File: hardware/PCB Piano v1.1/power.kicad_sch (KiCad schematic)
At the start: 51 parts, among them CON1 254, J1 USB_C_Receptacle_USB2.0_16P, J4 Conn_01x02_Pin, J5 Conn_01x02_Pin, SW1 MFS126D, U12 TLV73318PDBV, U3 BQ24072RGT, U8 TPS63001, U9 TPS61023

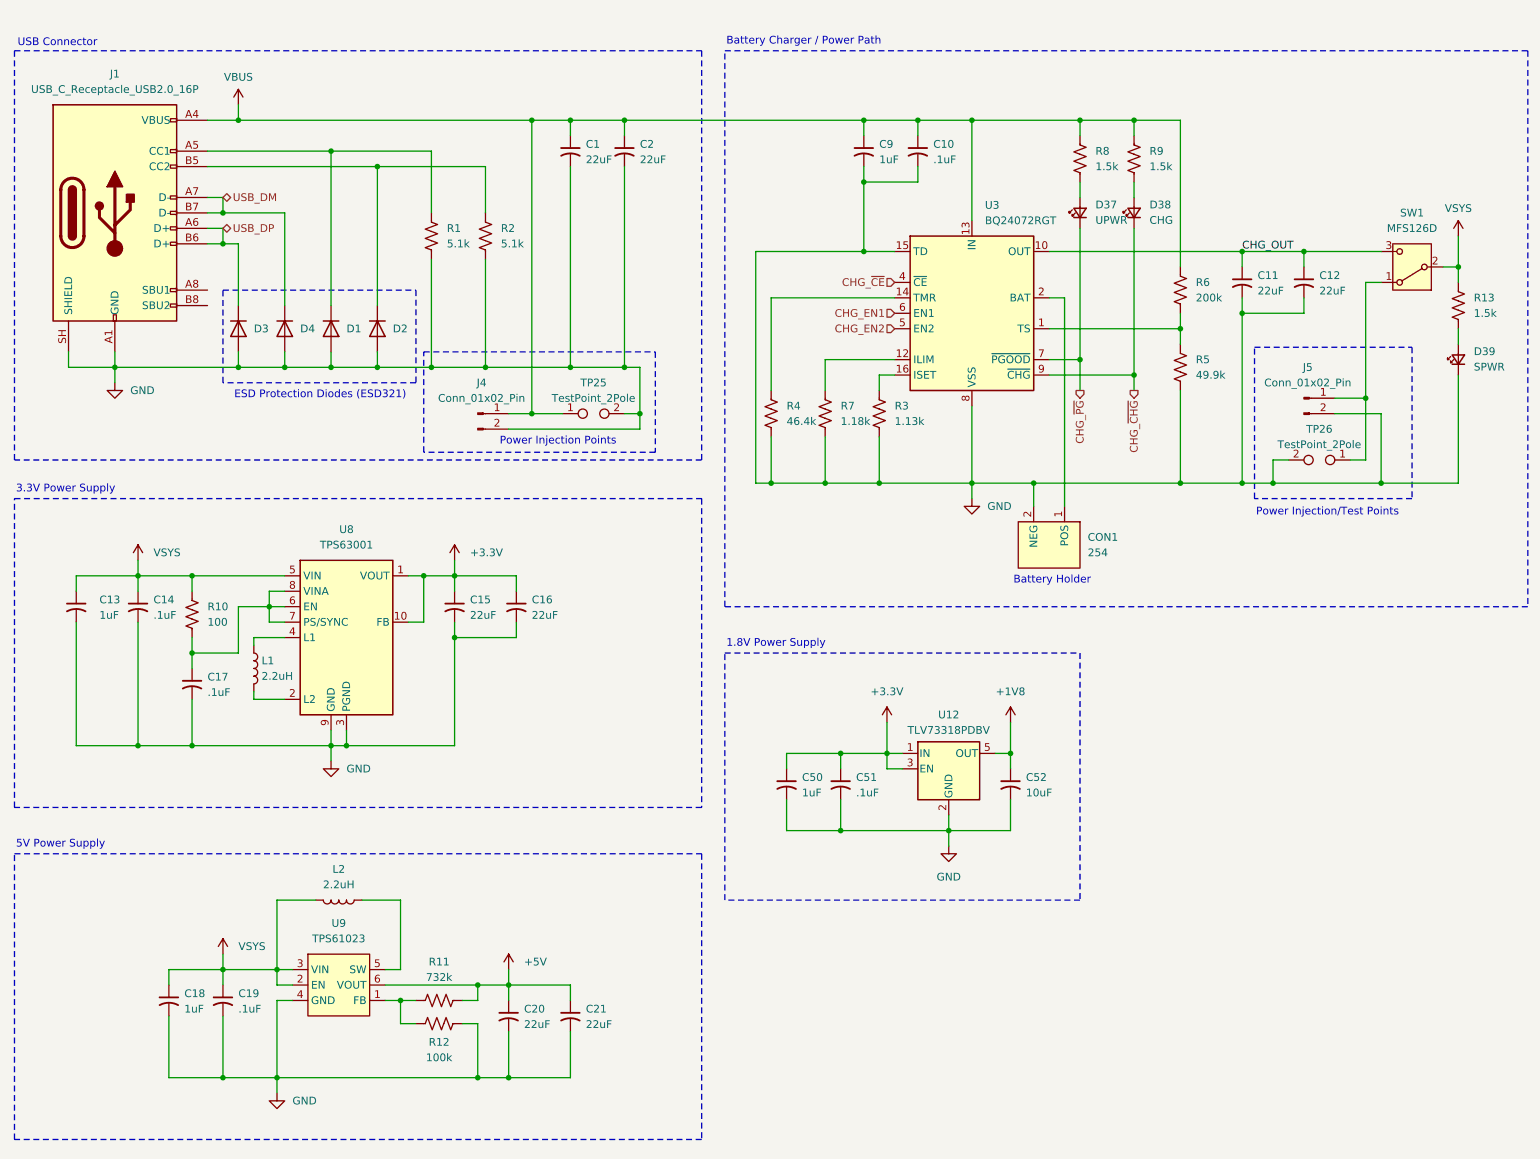
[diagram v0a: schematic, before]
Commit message: Development Phase - PCB Complete - ERC/DRC in progress
Development commit. PBC layout complete. ERC/DRC checks in progress. Swapped some connectors for JST connectors with Adafruit-style polarization.
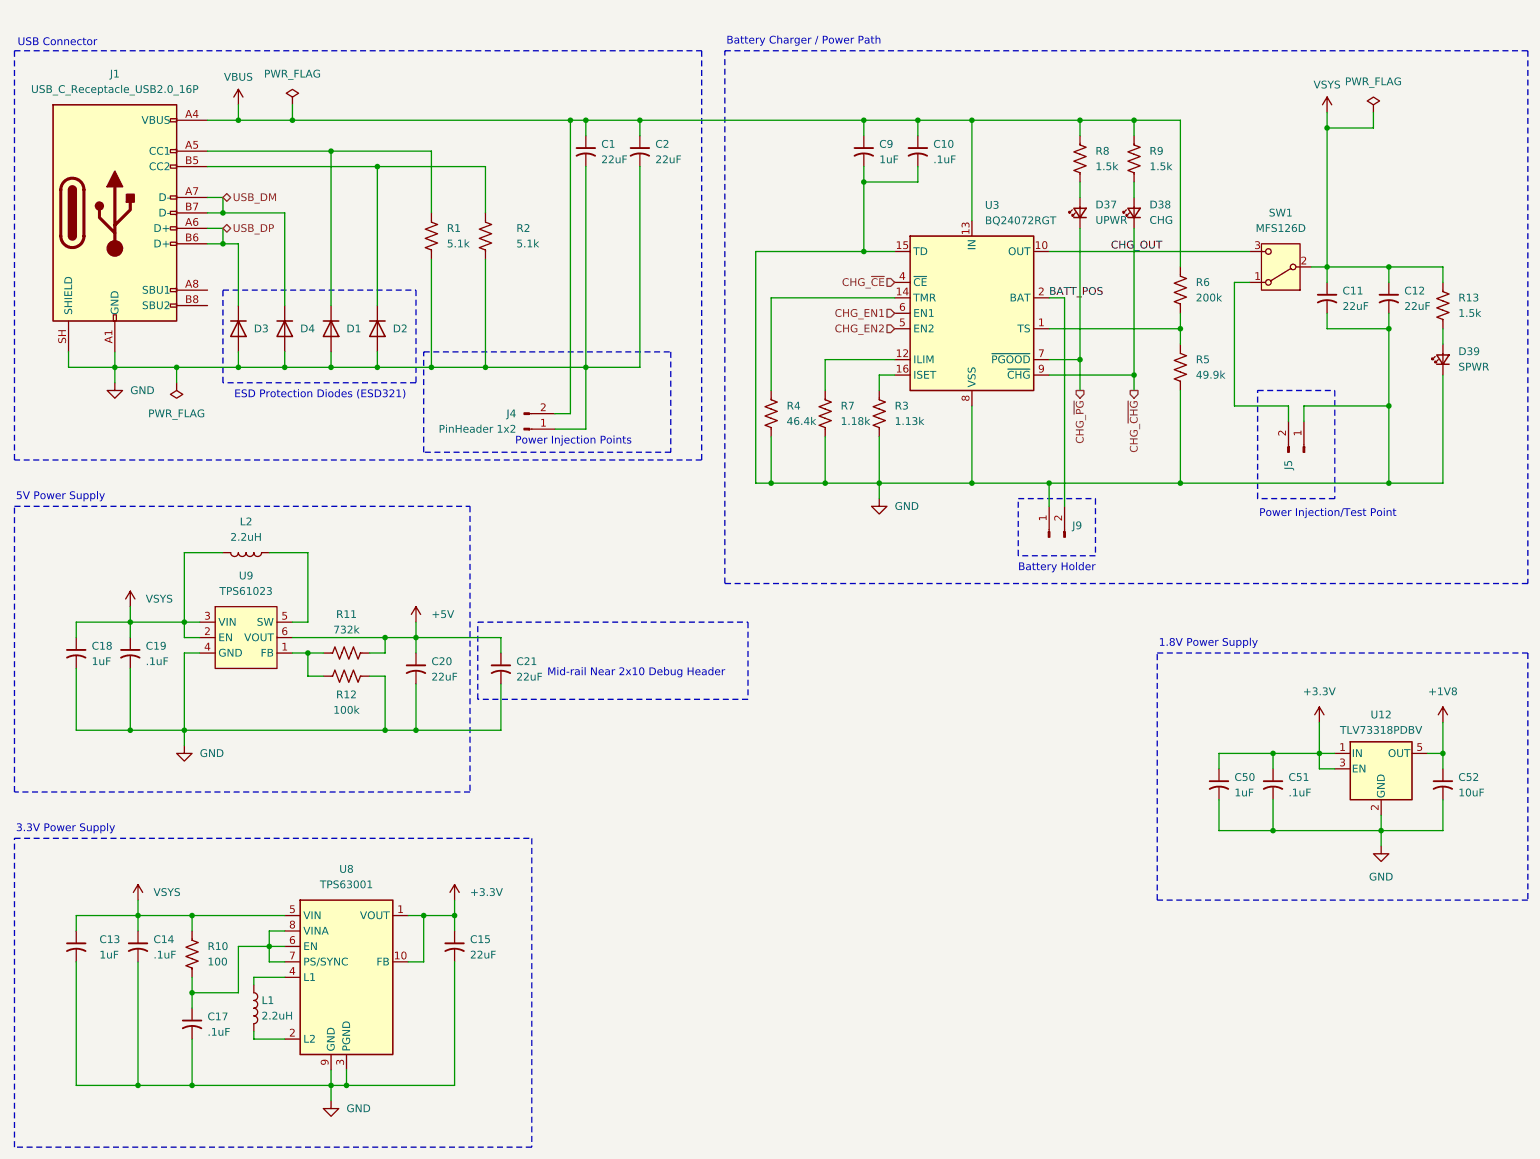
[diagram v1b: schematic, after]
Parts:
- removed C16: 22uF, Capacitor_Tantalum_SMD:CP_EIA-6032-20_AVX-F, symbol Device:C_Small_US
- removed CON1: 254, PCBPiano_Footprints:BatteryHolder_254Clips_18650Battery, symbol PCB Piano Symbols:254
- removed TP25, TP26: TestPoint_2Pole, PCBPiano_Footprints:TestPoint_2Pads_2.5mmx2.5mm_5mmSpacing, symbol Connector:TestPoint_2Pole
- added J9: (no value), Connector_JST:JST_PH_B2B-PH-SM4-TB_1x02-1MP_P2.00mm_Vertical, symbol Connector:Conn_01x02_Pin
- J4: value Conn_01x02_Pin -> PinHeader 1x2
- J5: value Conn_01x02_Pin -> (none)
- SW1: footprint PCBPiano_Footprints:SolderPoint_3Pads_2.54x2.54_5.08Spacing -> Connector_JST:JST_PH_B3B-PH-SM4-TB_1x03-1MP_P2.00mm_Vertical
- U9: symbol texas_instruments:TPS61023 -> PCB Piano Symbols:TPS61023
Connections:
- net CHG_OUT: no longer C11.1, C12.1
- net GND: now also J4.1 (Pin_1), J5.1 (Pin_1), J9.1 (Pin_1); no longer J4.2 (Pin_2), J5.2 (Pin_2)
- net VBUS: now also J4.2 (Pin_2); no longer J4.1 (Pin_1)
- net VSYS: now also C11.1, C12.1
- net BATT_POS: now reaches U3.2 (BAT), U3.3 (BAT)
- net BATT_POS: now also J9.2 (Pin_2)
- net at SW1.1 (A): now also J5.2 (Pin_2); no longer J5.1 (Pin_1)
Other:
- note added: "Mid-rail Near 2x10 Debug Header"
- note added: "Power Injection/Test Point"
- note removed: "Power Injection/Test Points"
- moved on the sheet: C1, C11, C12, C13, C14, C15, C17, C18, C19, C2, C20, C21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

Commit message: Firmware architecture complete - PCB revision with new charger.
Firmware Architecture Complete

- Added MP2724 charger driver
- Added TLV320DAC3100 driver
- Added MTCH2120 touch driver
- Added PCA9685 driver
- Added DotStar driver
- Added rotary encoder driver
- Added touch and LED maps
- Added control/audio/voice managers
- Added audio command queue
- Added Core1 audio architecture
- Added status LED system
- Added LED animation framework

Changes hardware schematic and PCB to accommodate a newer-style USB-C sink battery charger chip and USB data MUX to protect MCU while powered off.
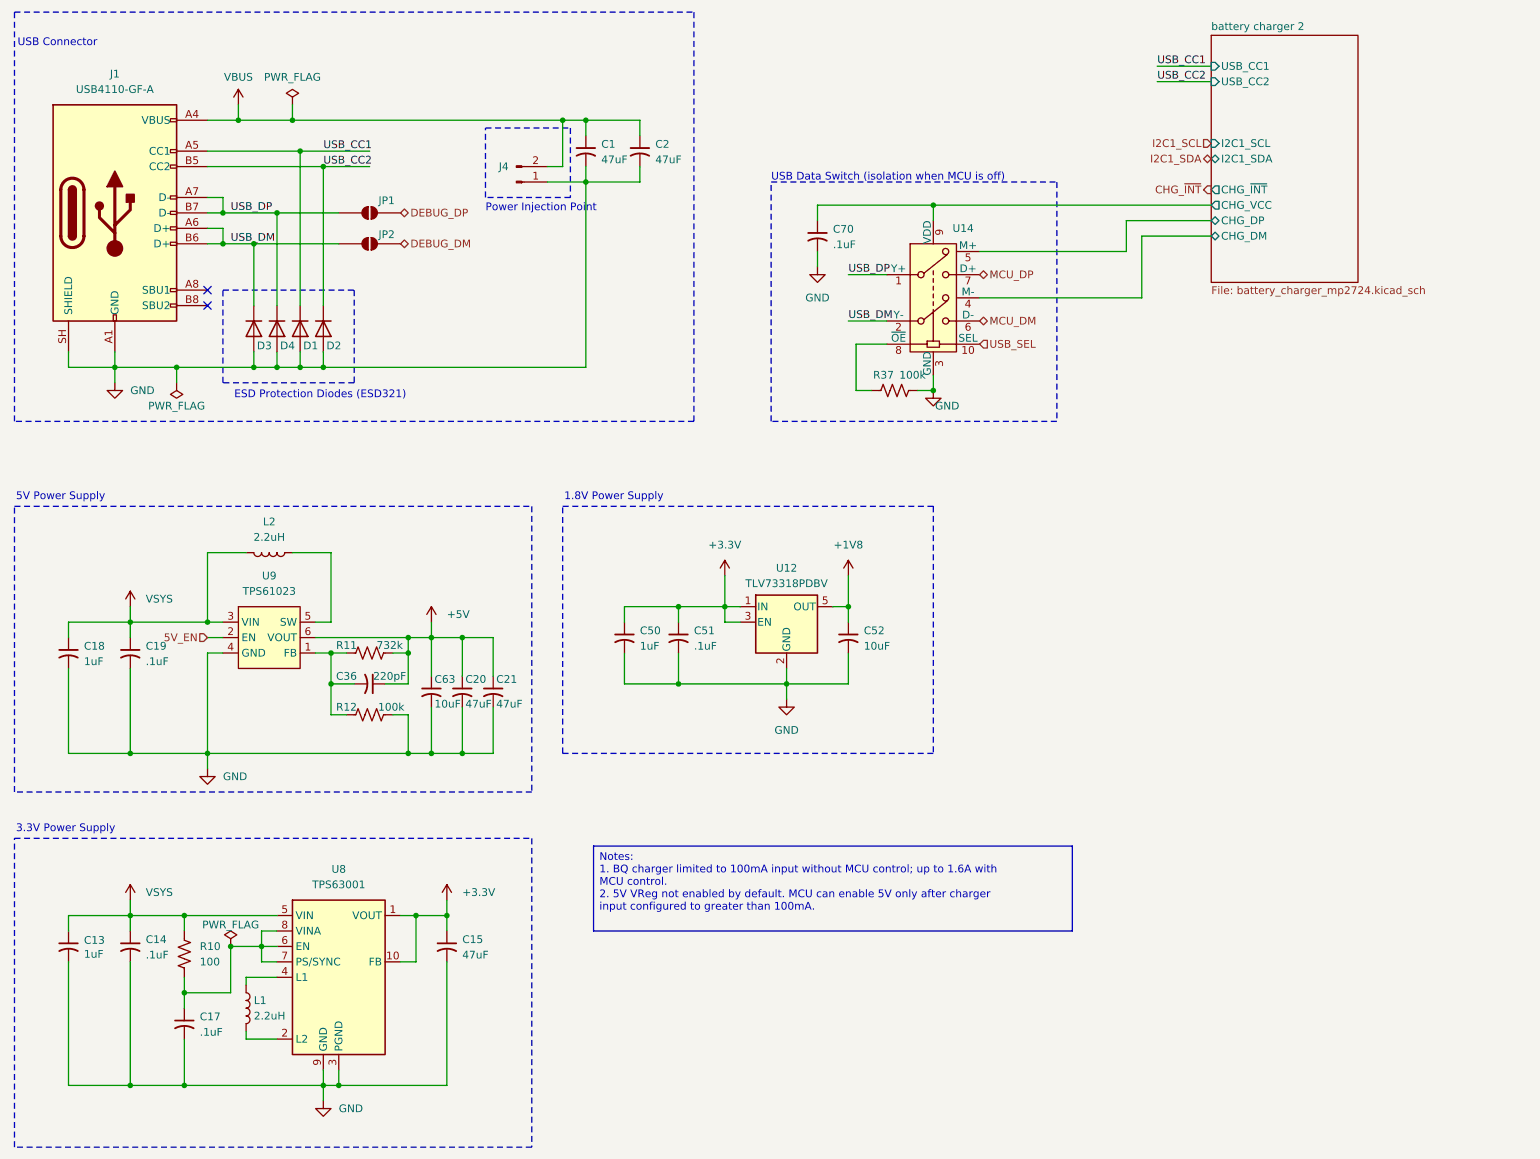
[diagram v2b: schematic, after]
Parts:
- removed C10: .1uF, Capacitor_SMD:C_0603_1608Metric, symbol Device:C_Small_US
- removed C11, C12: 22uF, Capacitor_Tantalum_SMD:CP_EIA-6032-20_AVX-F, symbol Device:C_Small_US
- removed C9: 1uF, Capacitor_SMD:C_0603_1608Metric, symbol Device:C_Small_US
- removed D37: UPWR, LED_SMD:LED_0603_1608Metric, symbol Device:LED_Small
- removed D38: CHG, LED_SMD:LED_0603_1608Metric, symbol Device:LED_Small
- removed D39: SPWR, LED_SMD:LED_0603_1608Metric, symbol Device:LED_Small
- removed J5: (no value), Connector_PinHeader_2.54mm:PinHeader_1x02_P2.54mm_Vertical_SMD_Pin1Left, symbol Connector:Conn_01x02_Pin
- removed J9: (no value), Connector_JST:JST_PH_B2B-PH-SM4-TB_1x02-1MP_P2.00mm_Vertical, symbol Connector:Conn_01x02_Pin
- removed R1, R2: 5.1k, Resistor_SMD:R_0603_1608Metric, symbol Device:R_US
- removed R13, R8, R9: 1.5k, Resistor_SMD:R_0603_1608Metric, symbol Device:R_US
- removed R3: 1.13k, Resistor_SMD:R_0603_1608Metric, symbol Device:R_US
- removed R4: 46.4k, Resistor_SMD:R_0603_1608Metric, symbol Device:R_US
- removed R5: 49.9k, Resistor_SMD:R_0603_1608Metric, symbol Device:R_US
- removed R6: 200k, Resistor_SMD:R_0603_1608Metric, symbol Device:R_US
- removed R7: 1.18k, Resistor_SMD:R_0603_1608Metric, symbol Device:R_US
- removed SW1: MFS126D, Connector_JST:JST_PH_B3B-PH-SM4-TB_1x03-1MP_P2.00mm_Vertical, symbol Switch:SW_SPDT
- removed U3: BQ24072RGT, Package_DFN_QFN:VQFN-16-1EP_3x3mm_P0.5mm_EP1.6x1.6mm, symbol Battery_Management:BQ24072RGT
- added C36: 220pF, Capacitor_SMD:C_0603_1608Metric, symbol Device:C_Small_US
- added C63: 10uF, Capacitor_SMD:C_0805_2012Metric, symbol Device:C_Small_US
- added C70: .1uF, Capacitor_SMD:C_0603_1608Metric, symbol Device:C_Small_US
- added JP1, JP2: SolderJumper_2_Open, Jumper:SolderJumper-2_P1.3mm_Open_RoundedPad1.0x1.5mm, symbol Jumper:SolderJumper_2_Open
- added R37: 100k, Resistor_SMD:R_0603_1608Metric, symbol Device:R_US
- added U14: PI3USB102G, PCBPiano_Footprints:TQFN-10_ZL_1.6x1.3mm_P0.4mm, symbol PCB_Piano_Symbols:Switch_USB_Data_Dual_SPDT_PI3USB102G
- C1, C15, C2, C20, C21: value 22uF -> 47uF; footprint Capacitor_Tantalum_SMD:CP_EIA-6032-20_AVX-F -> Capacitor_Tantalum_SMD:CP_EIA-3528-15_AVX-H
- C52: footprint Capacitor_SMD:C_0603_1608Metric -> Capacitor_SMD:C_0805_2012Metric
- D1, D2, D3, D4: value (none) -> ESD321; footprint Diode_SMD:D_SOD-523 -> PCBPiano_Footprints:D_SOD-523
- J1: value USB_C_Receptacle_USB2.0_16P -> USB4110-GF-A; footprint Connector_USB:USB_C_Receptacle_GCT_USB4110 -> PCBPiano_Footprints:USB_C_Receptacle_GCT_USB4110
- J4: value PinHeader 1x2 -> PinHeader 1x02 SMT
- L1: footprint Inductor_SMD:L_1008_2520Metric -> PCBPiano_Footprints:L_Bourns_SRP4020T_4.06x4.45x2.0mm
- L2: footprint Inductor_SMD:L_1008_2520Metric -> PCBPiano_Footprints:L_Pulse_BMRB00060630_7.3x6.6mm
- U8: footprint Package_SON:Texas_DRC0010J_ThermalVias -> PCBPiano_Footprints:Texas_DRC0010J
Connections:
- net +5V: now also C36.1, C63.1
- net GND: now also C63.2, C70.2, R37.1, U14.3 (GND)
- net USB_DM: now also D3.1 (K), J1.A6 (D+), J1.B6 (D+), JP2.1 (A), U14.2 (Y-); no longer D4.1 (K), J1.A7 (D-), J1.B7 (D-)
- net USB_DP: now also D4.1 (K), J1.A7 (D-), J1.B7 (D-), JP1.1 (A), U14.1 (Y+); no longer D3.1 (K), J1.A6 (D+), J1.B6 (D+)
- net VSYS: no longer U9.2 (EN)
- net USB_CC1: now reaches D1.1 (K), J1.A5 (CC1)
- net at R11.2, R12.2, U9.1 (FB): now also C36.2
- net USB_CC2: now reaches D2.1 (K), J1.B5 (CC2)
- new net: R37.2, U14.8 (~{OE})
- new net 5V_EN: U9.2 (EN)
- new net DEBUG_DM: JP2.2 (B)
- new net DEBUG_DP: JP1.2 (B)
- new net MCU_DM: U14.6 (D-)
- new net MCU_DP: U14.7 (D+)
- new net USB_SEL: U14.10 (SEL)
- new net battery charger 2/CHG_DM: U14.4 (M-)
- new net battery charger 2/CHG_DP: U14.5 (M+)
- new net battery charger 2/CHG_VCC: C70.1, U14.9 (VDD)
- no-connect marks 0 -> 2
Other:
- added sheet battery charger 2 (battery_charger_mp2724.kicad_sch)
- note added: "Power Injection Point"
- note added: "USB Data Switch (isolation when MCU is off)"
- note removed: "Battery Charger / Power Path"
- note removed: "Battery Holder"
- note removed: "Mid-rail Near 2x10 Debug Header"
- note removed: "Power Injection Points"
- note removed: "Power Injection/Test Point"
- moved on the sheet: C13, C14, C15, C17, C18, C20, C50, C51, C52, D1, D2, D3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

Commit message: PCB Finalized and Ordered. Firmware near completion.
PCB Finalized and Ordered. Final revisions included fixing bugs on some peripheral chips. Also added an RTC circuit after realizing the SD card could benefit from adding file timestamps.

Firmware near completion. Still need to finalize some SD card operations. Synth audio core is finished and all the board peripheral chip drivers were completed.
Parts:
- removed C2: 47uF, Capacitor_Tantalum_SMD:CP_EIA-3528-15_AVX-H, symbol Device:C_Small_US
- added C78, C79: 47uF, Capacitor_Tantalum_SMD:CP_EIA-3528-15_AVX-H, symbol Device:C_Small_US
- added D45: 3.3Vf, 104mcd, PCBPiano_Footprints:LED_0603_1608Metric, symbol Device:LED_Small
- added J5: PinHeader 1x02 SMT, Connector_PinHeader_2.54mm:PinHeader_1x02_P2.54mm_Vertical_SMD_Pin1Right, symbol Connector:Conn_01x02_Pin
- added R77: 1.5k, Resistor_SMD:R_0603_1608Metric, symbol Device:R_US
- added SW1: JST-PH 1x03 SMT, Connector_JST:JST_PH_B3B-PH-SM4-TB_1x03-1MP_P2.00mm_Vertical, symbol PCB Piano Symbols:SW_SPDT_MP
- C1: footprint Capacitor_Tantalum_SMD:CP_EIA-3528-15_AVX-H -> Capacitor_Tantalum_SMD:CP_EIA-7343-43_Kemet-X; DigiKey_Part_Number (none) -> TAJB476K010RNJ; Manufacturer Part Number (none) -> TAJB476K010RNJ; Volt Rating (none) -> 25V
- C13, C18, C50: DigiKey_Part_Number (none) -> 1276-1184-1-ND; Manufacturer Part Number (none) -> CL10B105KA8NNNC; Volt Rating (none) -> 10V
- C14, C17, C19, C51, C70: DigiKey_Part_Number (none) -> 1276-1935-2-ND; Manufacturer Part Number (none) -> CL10B104KB8NNWC; Volt Rating (none) -> 10V
- C15, C20, C21: DigiKey_Part_Number (none) -> TAJB476K010RNJ; Manufacturer Part Number (none) -> TAJB476K010RNJ; Volt Rating (none) -> 10V
- C36: DigiKey_Part_Number (none) -> 478-KGM15ACG1E221JTCT-ND; Manufacturer Part Number (none) -> KGM15ACG1E221JT; Volt Rating (none) -> 10V
- C52, C63: DigiKey_Part_Number (none) -> 490-10516-1-ND; Manufacturer Part Number (none) -> GRM21BR71A106KA73L GRM21BR71A106KA73L GRM21BR71A106KA73L GR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; Volt Rating (none) -> 10V
- D1, D2, D3, D4: DigiKey_Part_Number (none) -> ESD321; Manufacturer Part Number (none) -> ESD321
- J1: DigiKey_Part_Number (none) -> USB4110-GF-A; Manufacturer Part Number (none) -> USB4110-GF-A
- J4: footprint Connector_PinHeader_2.54mm:PinHeader_1x02_P2.54mm_Vertical_SMD_Pin1Left -> Connector_PinHeader_2.54mm:PinHeader_1x02_P2.54mm_Vertical_SMD_Pin1Right
- JP1, JP2: footprint Jumper:SolderJumper-2_P1.3mm_Open_RoundedPad1.0x1.5mm -> PCBPiano_Footprints:SolderJumper-2_P1.3mm_Open_RoundedPad1.0x1.5mm
- U12: value TLV73318PDBV -> 1.8V; DigiKey_Part_Number (none) -> TLV73318PDBV; Manufacturer Part Number (none) -> TLV73318PDBV
- U14: value PI3USB102G -> 1:2 USB MUX; DigiKey_Part_Number (none) -> PI3USB102G; Manufacturer Part Number (none) -> PI3USB102G
- U8: value TPS63001 -> 3.3V; DigiKey_Part_Number (none) -> TPS63001; Manufacturer Part Number (none) -> TPS63001
- U9: value TPS61023 -> 5V; DigiKey_Part_Number (none) -> TPS61023; Manufacturer Part Number (none) -> TPS61023
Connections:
- net DEBUG_DM: now also JP2.1 (A); no longer JP2.2 (B)
- net DEBUG_DP: now also JP1.1 (A); no longer JP1.2 (B)
- net GND: now also C78.2, C79.2, D45.1 (K), J5.1 (Pin_1), SW1.MP
- net USB_DM: now also JP2.2 (B); no longer JP2.1 (A)
- net USB_DP: now also JP1.2 (B); no longer JP1.1 (A)
- net VSYS: now also C78.1, C79.1, R77.1, SW1.2 (B)
- new net: D45.2 (A), R77.2
- new net: J5.2 (Pin_2), SW1.1 (A)
- new net CHG_OUT: SW1.3 (C)
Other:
- sheet battery charger 2 ports: added CHG_OUT; removed none
- moved on the sheet: C70, JP1, JP2
